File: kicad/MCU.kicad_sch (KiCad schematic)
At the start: 78 parts, among them J10 Display, J11 USB4215-03, J7 USART, J8 FAN, Q6 NX138AKR, Q7 NX138AKR, Q8 NX138AKR, SW1 RST, SW2 BOOT, SW3 ENC0 (Voltage), SW4 ENC1 (Current), U4 STM32F373C8Tx, U6 MCP9700A, Y1 Crystal

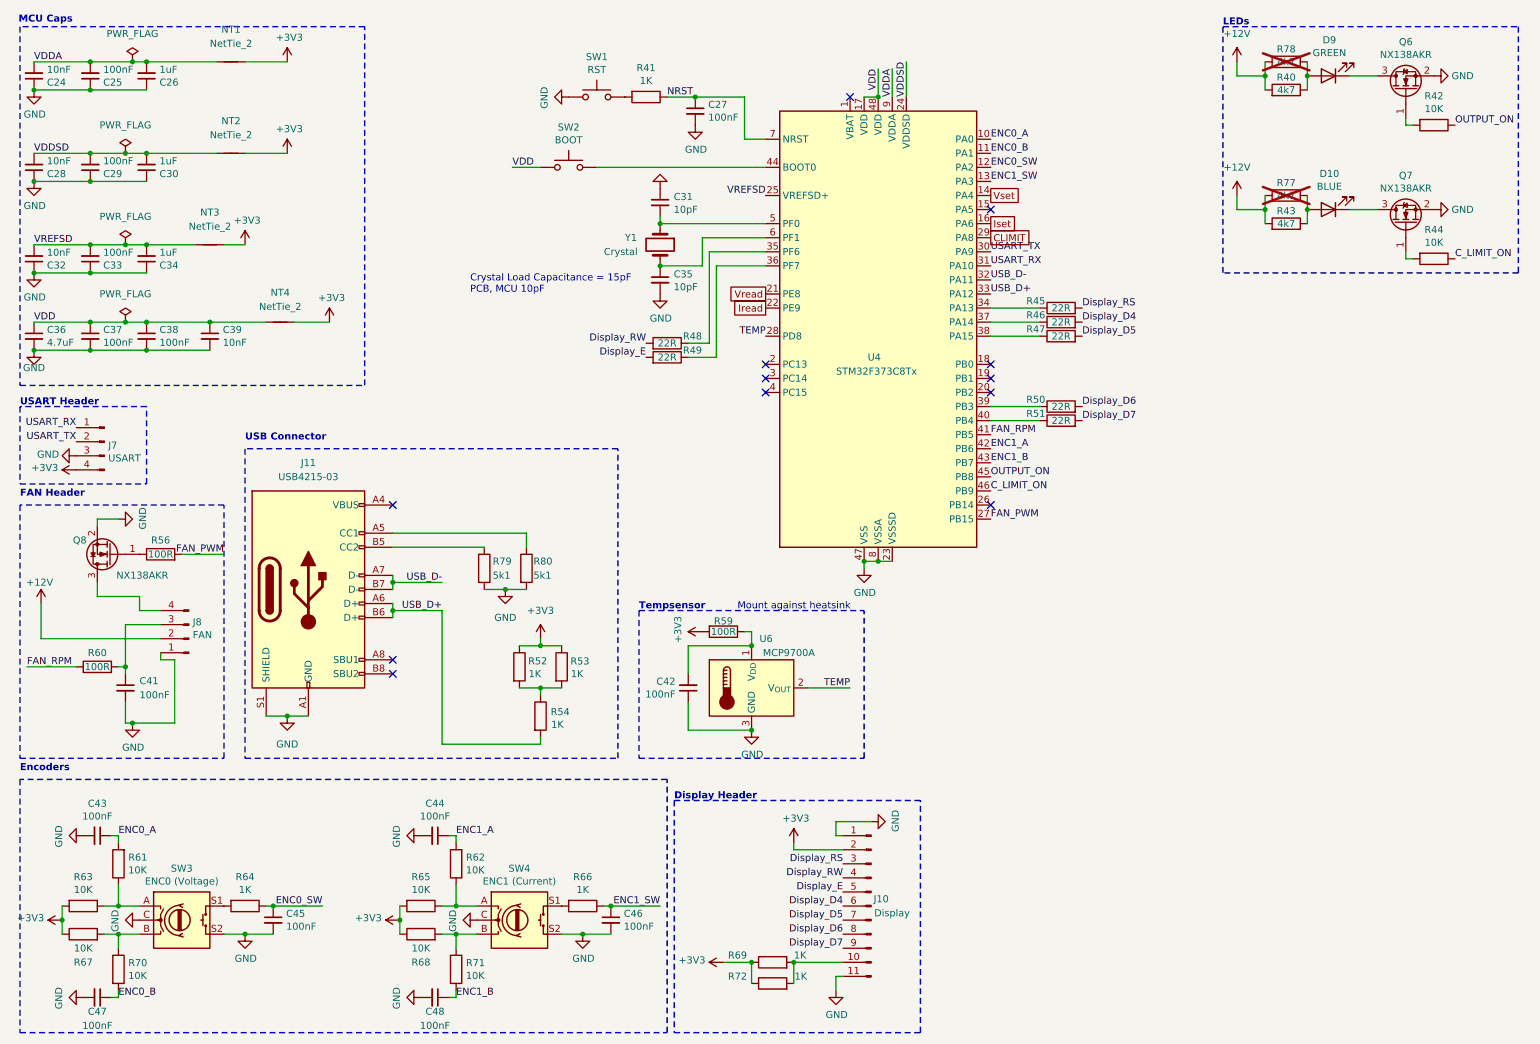
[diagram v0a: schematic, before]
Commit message: Added more caps on SMPS outputs
- Added pin header for BOOT and RST
- Re added USBLC6-2SC6
  - can be connected to VBUS or 3V3
- 0R option to connect usb shield to GND
- Added solder pad for 12V
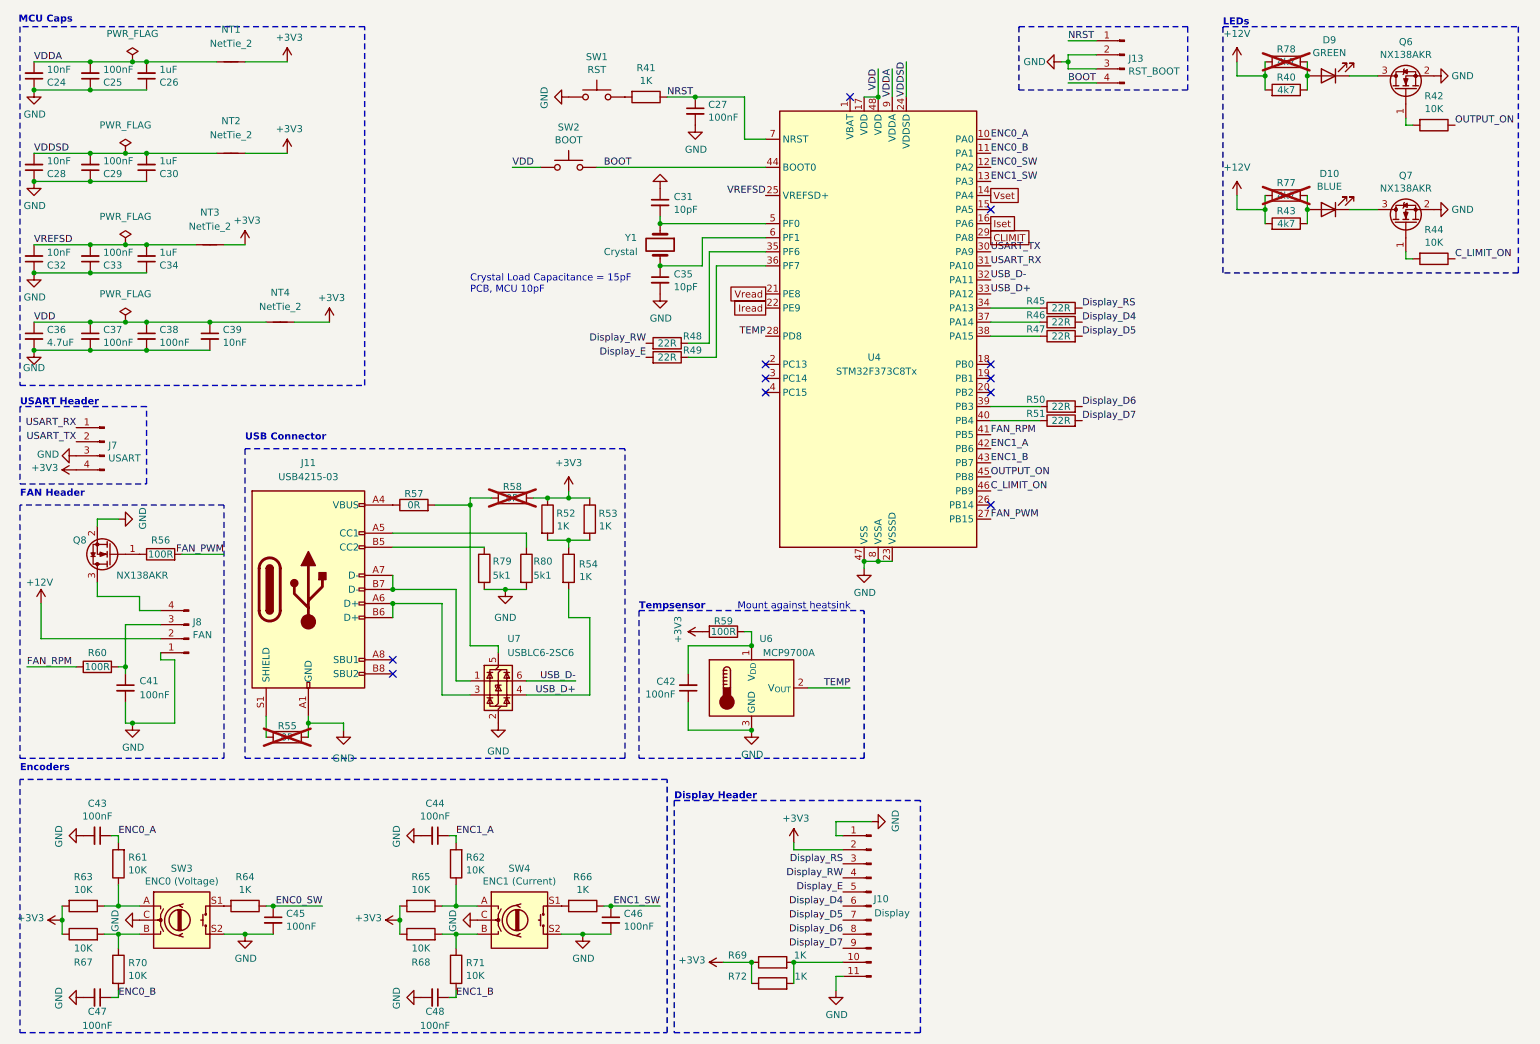
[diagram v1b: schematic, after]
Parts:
- added J13: RST_BOOT, Connector_PinHeader_2.54mm:PinHeader_1x04_P2.54mm_Vertical, symbol Connector:Conn_01x04_Pin
- added R55, R57, R58: 0R, symbol Device:R
- added U7: USBLC6-2SC6, Package_TO_SOT_SMD:SOT-23-6_Handsoldering, symbol Power_Protection:USBLC6-2SC6
- SW1, SW2: MPN LL3301NF065QG -> TS04-66-55-BK-100-SMT
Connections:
- net +3V3: now also R58.2
- net GND: now also J13.2 (Pin_2), J13.3 (Pin_3), R55.2, U7.2 (GND); no longer J11.S1 (SHIELD)
- net NRST: now also J13.1 (Pin_1)
- net USB_D+: now also U7.4 (I/O2); no longer J11.A6 (D+), J11.B6 (D+)
- net USB_D-: now also U7.6 (I/O1); no longer J11.A7 (D-), J11.B7 (D-)
- net BOOT: now reaches SW2.1, U4.44 (BOOT0)
- net BOOT: now also J13.4 (Pin_4)
- net at J11.A4 (VBUS), J11.A9 (VBUS), J11.B4 (VBUS)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: now also R57.1
- new net: R57.2, R58.1, U7.5 (VBUS)
- new net: J11.A7 (D-), J11.B7 (D-), U7.1 (I/O1)
- new net: J11.A6 (D+), J11.B6 (D+), U7.3 (I/O2)
- new net: J11.S1 (SHIELD), R55.1
- no-connect marks 12 -> 11
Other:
- moved on the sheet: R52, R53, R54

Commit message: Removed unnecessary caps and other shit
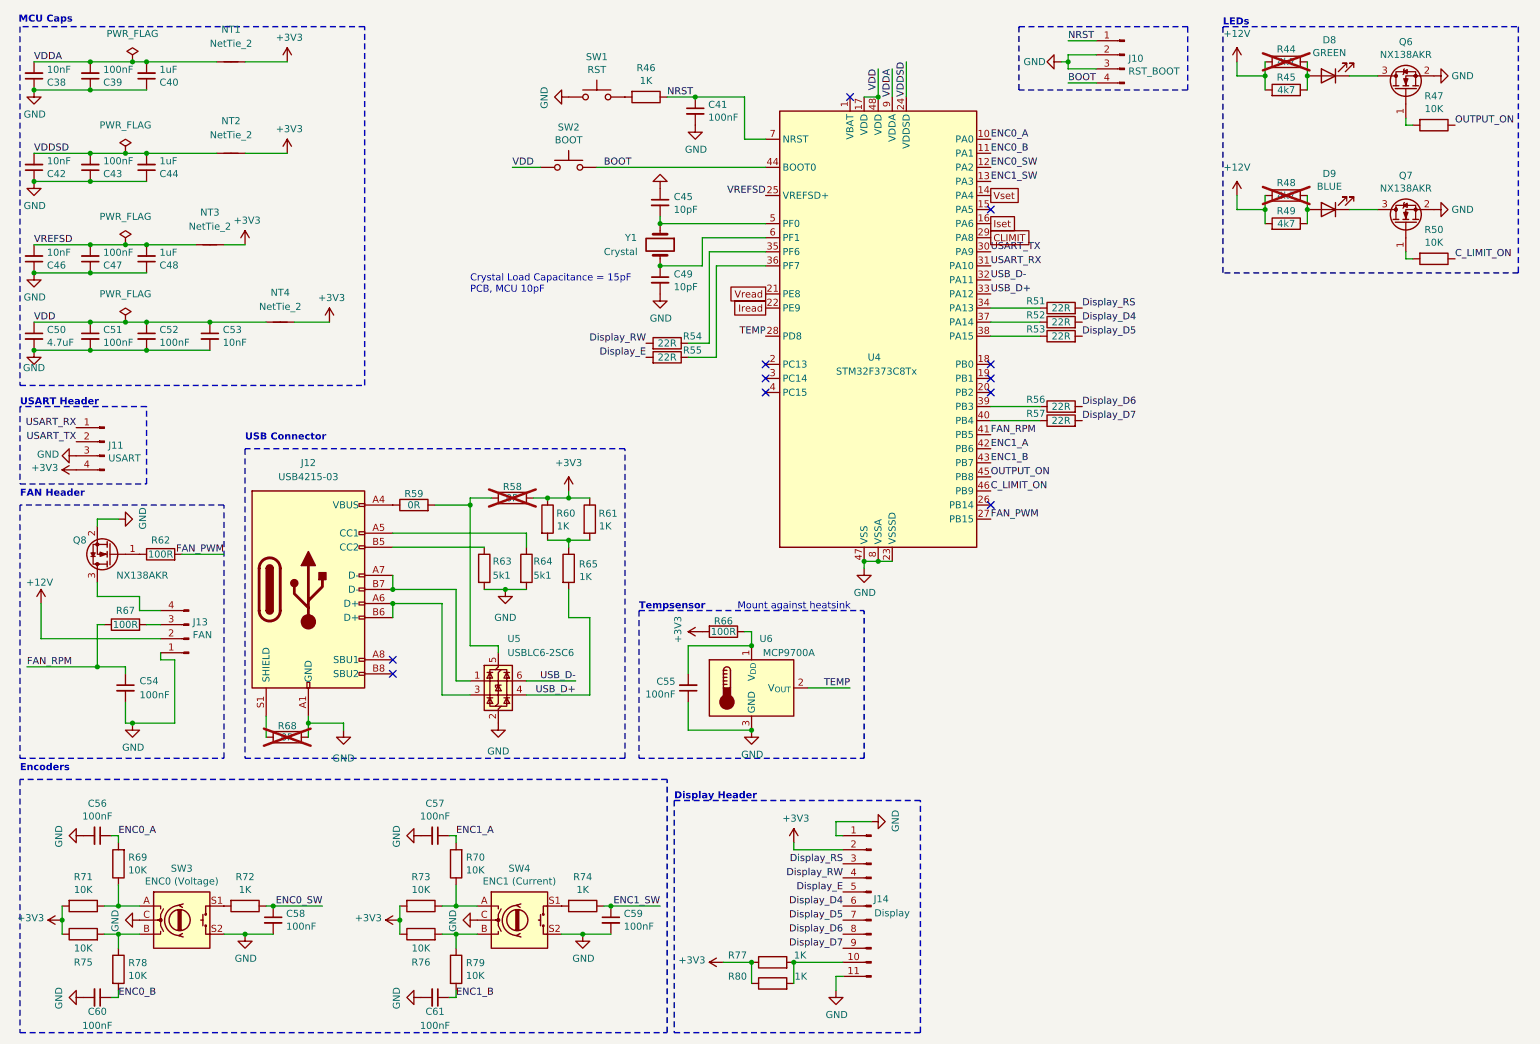
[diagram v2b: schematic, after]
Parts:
- R59: renamed from R57; footprint (none) -> Resistor_SMD:R_0805_2012Metric_Pad1.20x1.40mm_HandSolder
- renumbered C24 to C38, C25 to C39, C26 to C40, C27 to C41, C28 to C42, C29 to C43, C30 to C44, C31 to C45, C32 to C46, C33 to C47, C34 to C48, C35 to C49, C36 to C50, C37 to C51, C38 to C52, C39 to C53, C41 to C54, C42 to C55, C43 to C56, C44 to C57, C45 to C58, C46 to C59, C47 to C60, C48 to C61, D9 to D8, D10 to D9, J13 to J10, J7 to J11, J11 to J12, J8 to J13, J10 to J14, R78 to R44, R40 to R45, R41 to R46, R42 to R47, R77 to R48, R43 to R49, R44 to R50, R45 to R51, R46 to R52, R47 to R53, R48 to R54, R49 to R55, R50 to R56, R51 to R57, R52 to R60, R53 to R61, R56 to R62, R79 to R63, R80 to R64, R54 to R65, R59 to R66, R60 to R67, R55 to R68, R61 to R69, R62 to R70, R63 to R71, R64 to R72, R65 to R73, R66 to R74, R67 to R75, R68 to R76, R69 to R77, R70 to R78, R71 to R79, R72 to R80, U7 to U5
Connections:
- net FAN_RPM: now also C54.1
- net at J13.3 (Pin_3), R67.2: no longer C54.1
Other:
- moved on the sheet: R67

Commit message: Moved FAN_RPM to pin PB14
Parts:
- R58, R68: footprint (none) -> Resistor_SMD:R_0805_2012Metric_Pad1.20x1.40mm_HandSolder
- renumbered C38 to C27, C39 to C28, C40 to C29, C41 to C30, C42 to C31, C43 to C32, C44 to C33, C45 to C34, C46 to C35, C47 to C36, C48 to C37, C49 to C38, C50 to C39, C51 to C40, C52 to C41, C53 to C42, C54 to C43, C55 to C44, C56 to C45, C57 to C46, C58 to C47, C59 to C48, C60 to C49, C61 to C50, R67 to R66, R66 to R67
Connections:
- net FAN_RPM: now also U4.26 (PB14); no longer U4.41 (PB5)
